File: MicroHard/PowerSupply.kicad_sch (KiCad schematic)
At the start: 14 parts, among them U1 TPS54325

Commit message: feat: finished power supply
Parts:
- added C1, C16, C18, C2: 22u, symbol Device:C
- added C11: 1u, symbol Device:C
- added C12, C14, C7, C8: 100n, symbol Device:C
- added C13, C5: 10u, symbol Device:C
- added FB1: FerriteBead, symbol Device:FerriteBead
- added L1: 1.5u, symbol Device:L
- added L3: 2.2u, symbol Device:L
- added R1: 30.1k, symbol Device:R
- added R2, R8: 22.1k, symbol Device:R
- added R6: 100k, symbol Device:R
- added R7: 73.2k, symbol Device:R
- added R9: 1, symbol Device:R
- L2: value L -> 1.5u
- U2: value ~ -> TPS54294
- renumbered R1 to R5
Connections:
- net GND: now also U2.13 (PGND2), U2.17 (PwPd), U2.4 (PGND1), U2.8 (GND), C1.2, C11.2, C13.1, C14.1, C16.2, C18.2, C2.2, C5.1, C7.1, R2.2, R8.2
- net POWER_IN: now also U2.1 (VIN1), U2.16 (VIN2), C13.2, C14.2, C5.2, C7.2
- net at U2.10 (VFB2): now also R7.2, R8.1
- net EN3.3V: now reaches U2.12 (EN2)
- net EN3.3V: now also U2.6 (PG1), R6.2
- net at U2.14 (SW2): now also C12.1, L3.2
- net at U2.15 (VBST2): now also C12.2
- net at U2.2 (VBST1): now also C8.2
- net at U2.3 (SW1): now also C8.1, L1.2
- net EN1.8V: now reaches U2.5 (EN1)
- net EN1.8V: now also R5.1, U1.6 (PG)
- net at U2.7 (VFB1): now also R1.2, R2.1
- net at U2.9 (VREG5): now also C11.1, R6.1
- net +1.0VO renamed +1.0V
- new net: FB1.2, R9.1
- new net +1.8V: C1.1, C2.1, L1.1, R1.1
- new net +3.3V: C16.1, C18.1, FB1.1, L3.1, R7.1
- new net +3.3VA: R9.2
- no-connect marks 0 -> 1
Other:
- note added: "Ip>2.8A, Irms>2.1A"
- note added: "Ip>2.9A, Irms>2.1A"
- moved on the sheet: C10, C15, C17, C19, C3, C4, C6, C9, L2, R3, R4, R5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

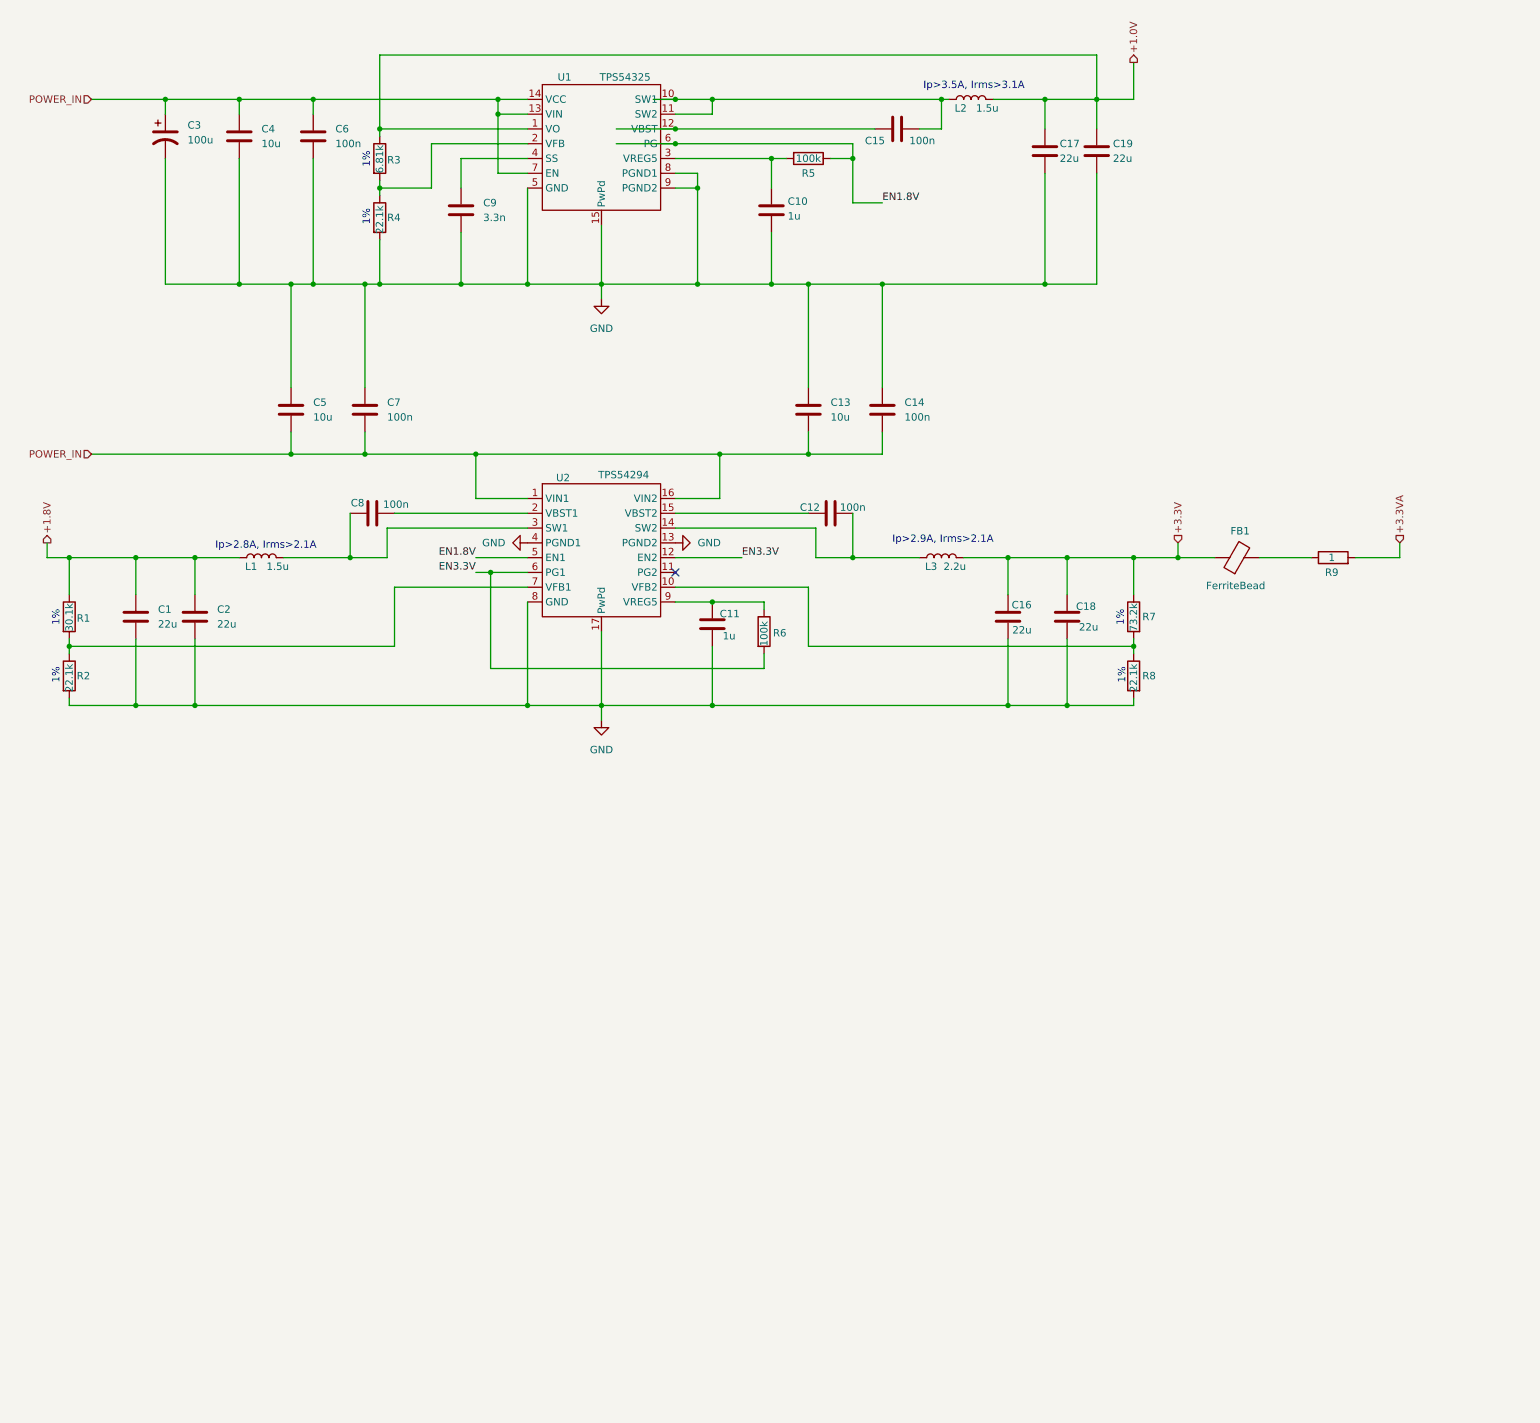
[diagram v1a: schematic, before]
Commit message: fix: powersupply passes ERV
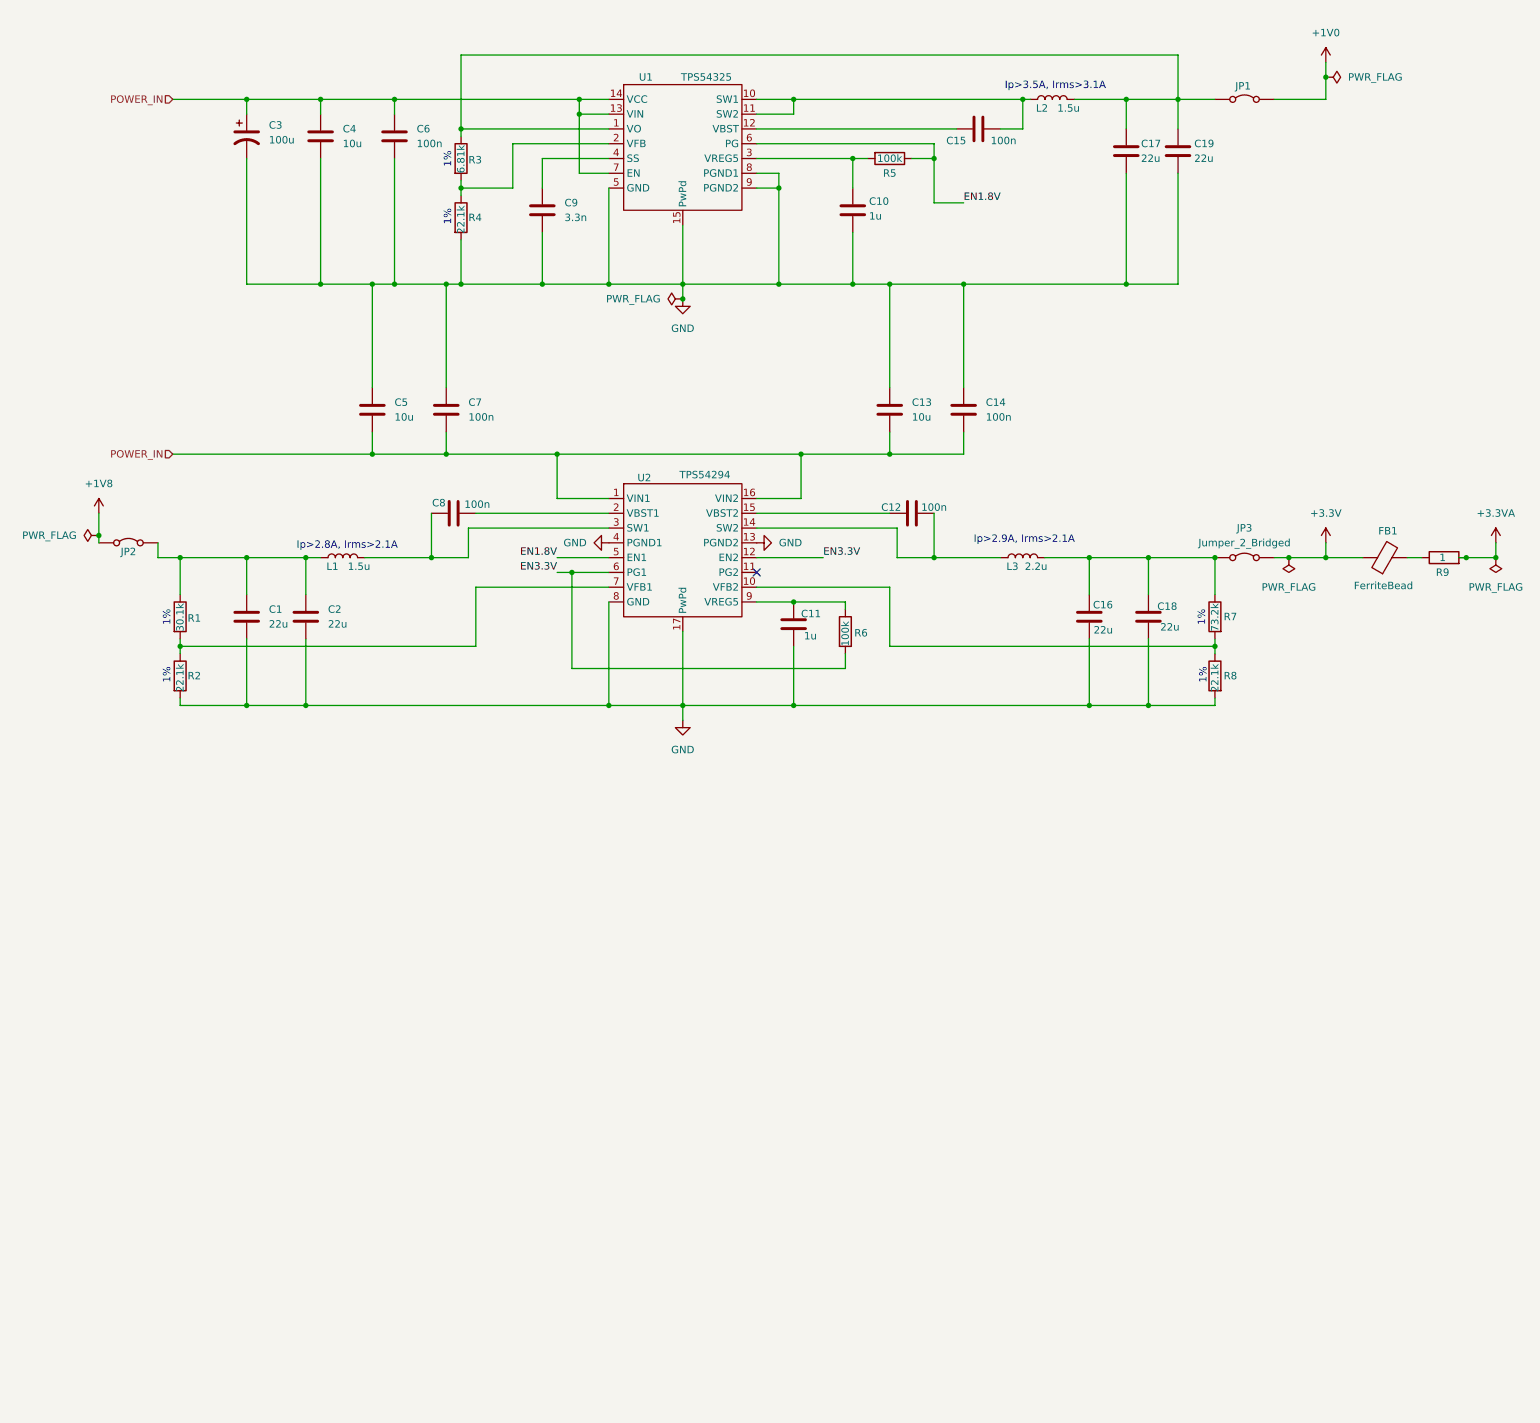
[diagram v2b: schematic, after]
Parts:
- added JP1, JP2, JP3: Jumper_2_Bridged, symbol Jumper:Jumper_2_Bridged
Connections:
- net +3.3V: now also JP3.2 (B); no longer C16.1, C18.1, L3.1, R7.1
- net +1.0V: no longer names the net of C17.1, C19.1, L2.2, R3.1, U1.1 (VO)
- net +1.0V: now also JP1.1 (A)
- net +1.8V: no longer names the net of C1.1, C2.1, L1.1, R1.1
- net +1.8V: now also JP2.2 (B)
- new net: C16.1, C18.1, JP3.1 (A), L3.1, R7.1
- new net +1V0: JP1.2 (B)
- new net +1V8: JP2.1 (A)
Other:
- moved on the sheet: C1, C10, C11, C12, C13, C14, C15, C16, C17, C18, C19, C2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

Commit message: feat: VGA out lines from FPGA drawn
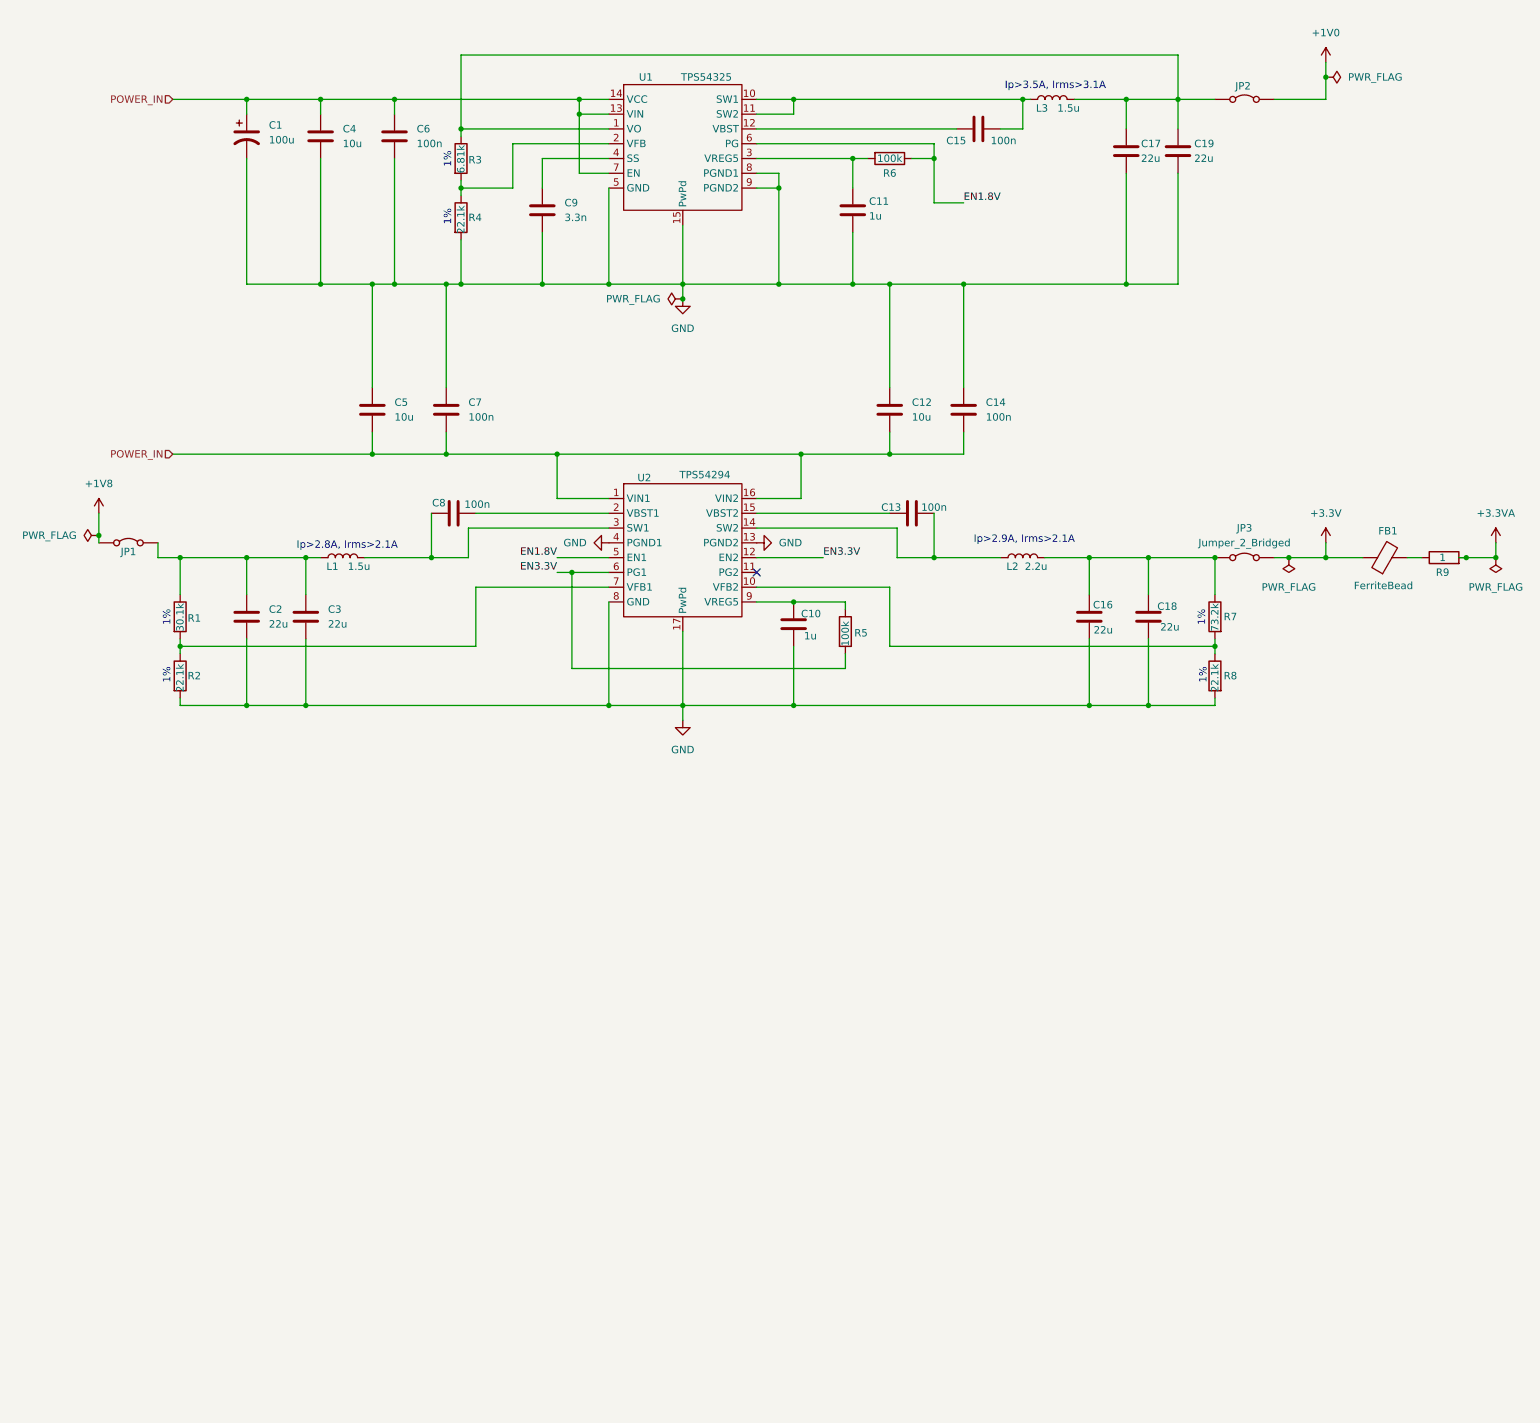
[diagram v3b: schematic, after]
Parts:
- renumbered C3 to C1, C11 to C10, C10 to C11, C13 to C12, C12 to C13, C1 to C2, C2 to C3, JP2 to JP1, JP1 to JP2, L3 to L2, L2 to L3, R6 to R5, R5 to R6
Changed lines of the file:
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@@
 		(on_board yes)
 		(dnp no)
-		(property "Reference" "C12"
+		(property "Reference" "C13"
 			(at 170.434 109.474 90)
 			(effects
@@
 			(project "MicroHard"
 				(path "/578bd531-a491-4b15-a479-460d159ffc14/f6ee64bd-5b5d-4329-b744-4c552611a962"
-					(reference "C12")
+					(reference "C13")
 					(unit 1)
 				)
@@
 		(dnp no)
 		(fields_autoplaced yes)
-		(property "Reference" "#PWR03"
+		(property "Reference" "#PWR02"
 			(at 115.57 115.57 0)
 			(effects
@@
 			(project "MicroHard"
 				(path "/578bd531-a491-4b15-a479-460d159ffc14/f6ee64bd-5b5d-4329-b744-4c552611a962"
-					(reference "#PWR03")
+					(reference "#PWR02")
 					(unit 1)
 				)
@@
 		(on_board yes)
 		(dnp no)
-		(property "Reference" "JP2"
+		(property "Reference" "JP1"
 			(at 39.37 117.094 0)
 			(effects
@@
 			(project ""
 				(path "/578bd531-a491-4b15-a479-460d159ffc14/f6ee64bd-5b5d-4329-b744-4c552611a962"
-					(reference "JP2")
+					(reference "JP1")
 					(unit 1)
 				)
@@
 		(on_board yes)
 		(dnp no)
-		(property "Reference" "R6"
+		(property "Reference" "R5"
 			(at 164.084 131.064 0)
 			(effects
@@
 			(project ""
 				(path "/578bd531-a491-4b15-a479-460d159ffc14/f6ee64bd-5b5d-4329-b744-4c552611a962"
-					(reference "R6")
+					(reference "R5")
 					(unit 1)
 				)
@@
 		(dnp no)
 		(fields_autoplaced yes)
-		(property "Reference" "C13"
+		(property "Reference" "C12"
 			(at 173.99 91.4399 0)
 			(effects
@@
 			(project "MicroHard"
 				(path "/578bd531-a491-4b15-a479-460d159ffc14/f6ee64bd-5b5d-4329-b744-4c552611a962"
-					(reference "C13")
+					(reference "C12")
 					(unit 1)
 				)
@@
 		(dnp no)
 		(fields_autoplaced yes)
-		(property "Reference" "#FLG05"
+		(property "Reference" "#FLG03"
 			(at 132.715 73.66 0)
 			(effects
@@
 			(project ""
 				(path "/578bd531-a491-4b15-a479-460d159ffc14/f6ee64bd-5b5d-4329-b744-4c552611a962"
-					(reference "#FLG05")
+					(reference "#FLG03")
 					(unit 1)
 				)
@@
 		(dnp no)
 		(fields_autoplaced yes)
-		(property "Reference" "#PWR02"
+		(property "Reference" "#PWR04"
 			(at 134.62 152.4 0)
 			(effects
@@
 			(project "MicroHard"
 				(path "/578bd531-a491-4b15-a479-460d159ffc14/f6ee64bd-5b5d-4329-b744-4c552611a962"
-					(reference "#PWR02")
+					(reference "#PWR04")
 					(unit 1)
 				)
@@
 		(on_board yes)
 		(dnp no)
-		(property "Reference" "C10"
+		(property "Reference" "C11"
 			(at 166.624 56.896 0)
 			(effects
@@
 			(project ""
 				(path "/578bd531-a491-4b15-a479-460d159ffc14/f6ee64bd-5b5d-4329-b744-4c552611a962"
-					(reference "C10")
+					(reference "C11")
 					(unit 1)
 				)
@@
 		(on_board yes)
 		(dnp no)
-		(property "Reference" "JP1"
+		(property "Reference" "JP2"
 			(at 230.886 37.084 0)
 			(effects
@@
 			(project ""
 				(path "/578bd531-a491-4b15-a479-460d159ffc14/f6ee64bd-5b5d-4329-b744-4c552611a962"
-					(reference "JP1")
+					(reference "JP2")
 					(unit 1)
 				)
@@
 		(dnp no)
 		(fields_autoplaced yes)
-		(property "Reference" "#FLG03"
+		(property "Reference" "#FLG02"
 			(at 32.385 114.3 0)
 			(effects
@@
 			(project ""
 				(path "/578bd531-a491-4b15-a479-460d159ffc14/f6ee64bd-5b5d-4329-b744-4c552611a962"
-					(reference "#FLG03")
+					(reference "#FLG02")
 					(unit 1)
 				)
@@
 		(dnp no)
 		(fields_autoplaced yes)
-		(property "Reference" "C1"
+		(property "Reference" "C2"
 			(at 63.5 126.9999 0)
 			(effects
@@
 			(project "MicroHard"
 				(path "/578bd531-a491-4b15-a479-460d159ffc14/f6ee64bd-5b5d-4329-b744-4c552611a962"
-					(reference "C1")
+					(reference "C2")
 					(unit 1)
 				)
@@
 		(dnp no)
 		(fields_autoplaced yes)
-		(property "Reference" "#PWR01"
+		(property "Reference" "#PWR03"
 			(at 134.62 80.01 0)
 			(effects
@@
 			(project ""
 				(path "/578bd531-a491-4b15-a479-460d159ffc14/f6ee64bd-5b5d-4329-b744-4c552611a962"
-					(reference "#PWR01")
+					(reference "#PWR03")
 					(unit 1)
 				)
@@
 		(dnp no)
 		(fields_autoplaced yes)
-		(property "Reference" "C2"
+		(property "Reference" "C3"
 			(at 73.66 126.9999 0)
 			(effects
@@
 			(project "MicroHard"
 				(path "/578bd531-a491-4b15-a479-460d159ffc14/f6ee64bd-5b5d-4329-b744-4c552611a962"
-					(reference "C2")
+					(reference "C3")
 					(unit 1)
 				)
@@
 		(on_board yes)
 		(dnp no)
-		(property "Reference" "C11"
+		(property "Reference" "C10"
 			(at 154.94 127.762 0)
 			(effects
@@
 			(project ""
 				(path "/578bd531-a491-4b15-a479-460d159ffc14/f6ee64bd-5b5d-4329-b744-4c552611a962"
-					(reference "C11")
+					(reference "C10")
 					(unit 1)
 				)
@@
 		(on_board yes)
 		(dnp no)
-		(property "Reference" "L3"
+		(property "Reference" "L2"
 			(at 191.262 119.634 90)
 			(effects
@@
 			(project "MicroHard"
 				(path "/578bd531-a491-4b15-a479-460d159ffc14/f6ee64bd-5b5d-4329-b744-4c552611a962"
-					(reference "L3")
+					(reference "L2")
 					(unit 1)
 				)
@@
 		(dnp no)
 		(fields_autoplaced yes)
-		(property "Reference" "#FLG02"
+		(property "Reference" "#FLG05"
 			(at 247.015 35.56 0)
 			(effects
@@
 			(project ""
 				(path "/578bd531-a491-4b15-a479-460d159ffc14/f6ee64bd-5b5d-4329-b744-4c552611a962"
-					(reference "#FLG02")
+					(reference "#FLG05")
 					(unit 1)
 				)
@@
 		(dnp no)
 		(fields_autoplaced yes)
-		(property "Reference" "#PWR05"
+		(property "Reference" "#PWR06"
 			(at 245.11 36.83 0)
 			(effects
@@
 			(project ""
 				(path "/578bd531-a491-4b15-a479-460d159ffc14/f6ee64bd-5b5d-4329-b744-4c552611a962"
-					(reference "#PWR05")
+					(reference "#PWR06")
 					(unit 1)
 				)
@@
 		(on_board yes)
 		(dnp no)
-		(property "Reference" "R5"
+		(property "Reference" "R6"
 			(at 170.18 52.07 90)
 			(effects
@@
 			(project ""
 				(path "/578bd531-a491-4b15-a479-460d159ffc14/f6ee64bd-5b5d-4329-b744-4c552611a962"
-					(reference "R5")
+					(reference "R6")
 					(unit 1)
 				)
@@
 		(on_board yes)
 		(dnp no)
-		(property "Reference" "L2"
+		(property "Reference" "L3"
 			(at 196.342 40.894 90)
 			(effects
@@
 			(project ""
 				(path "/578bd531-a491-4b15-a479-460d159ffc14/f6ee64bd-5b5d-4329-b744-4c552611a962"
-					(reference "L2")
+					(reference "L3")
 					(unit 1)
 				)
@@
 		(dnp no)
 		(fields_autoplaced yes)
-		(property "Reference" "#PWR06"
+		(property "Reference" "#PWR01"
 			(at 34.29 114.3 0)
 			(effects
@@
 			(project ""
 				(path "/578bd531-a491-4b15-a479-460d159ffc14/f6ee64bd-5b5d-4329-b744-4c552611a962"
-					(reference "#PWR06")
+					(reference "#PWR01")
 					(unit 1)
 				)
@@
 		(dnp no)
 		(fields_autoplaced yes)
-		(property "Reference" "#PWR04"
+		(property "Reference" "#PWR05"
 			(at 153.67 115.57 0)
 			(effects
@@
 			(project "MicroHard"
 				(path "/578bd531-a491-4b15-a479-460d159ffc14/f6ee64bd-5b5d-4329-b744-4c552611a962"
-					(reference "#PWR04")
+					(reference "#PWR05")
 					(unit 1)
 				)
@@
 		(on_board yes)
 		(dnp no)
-		(property "Reference" "C3"
+		(property "Reference" "C1"
 			(at 63.5 43.8149 0)
 			(effects
@@
 			(project ""
 				(path "/578bd531-a491-4b15-a479-460d159ffc14/f6ee64bd-5b5d-4329-b744-4c552611a962"
-					(reference "C3")
-					(unit 1)
-				)
+					(reference "C1")
+					(unit 1)
+				)
